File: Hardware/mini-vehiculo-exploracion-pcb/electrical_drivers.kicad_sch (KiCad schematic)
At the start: 13 parts, among them IC1 MAX8891EXK33_V+T, U1 TPS561208DDCR

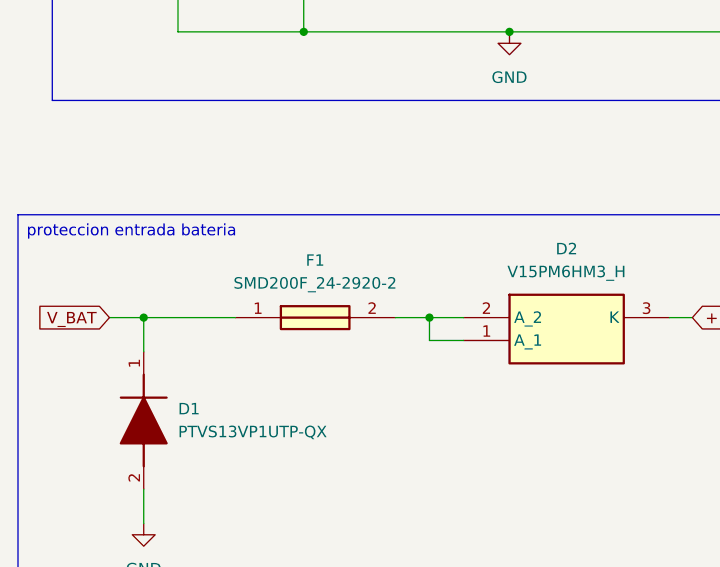
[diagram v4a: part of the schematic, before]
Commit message: actualizacion fusible drivers
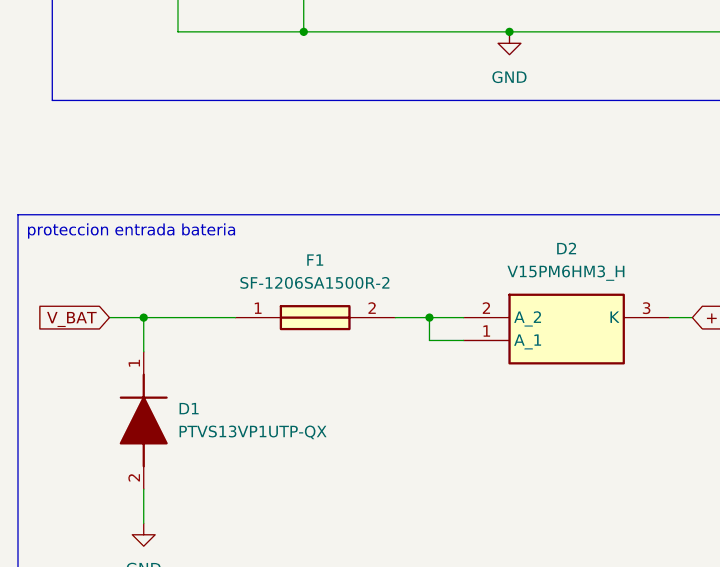
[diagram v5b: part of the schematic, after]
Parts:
- removed F1: SMD200F_24-2920-2, SMD200F2429202, symbol SMD200F_24-2920-2:SMD200F_24-2920-2
- added F1: SF-1206SA1500R-2, SF1206SA1500R2, symbol SF-1206SA1500R-2:SF-1206SA1500R-2
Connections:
- net V_BAT: now also F1.1
- net at D2.1 (A_1), D2.2 (A_2): now also F1.2
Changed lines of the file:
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@@
+	)
+	(symbol
+		(lib_id "SF-1206SA1500R-2:SF-1206SA1500R-2")
+		(at 41.91 96.52 0)
+		(unit 1)
+		(exclude_from_sim no)
+		(in_bom yes)
+		(on_board yes)
+		(dnp no)
+		(fields_autoplaced yes)
+		(property "Reference" "F1"
+			(at 50.8 90.17 0)
+			(effects
+				(font
+					(size 1.27 1.27)
+				)
+			)
+		)
+		(property "Value" "SF-1206SA1500R-2"
+			(at 50.8 92.71 0)
+			(effects
+				(font
+					(size 1.27 1.27)
+				)
+			)
+		)
+		(property "Footprint" "SF1206SA1500R2"
+			(at 55.88 192.71 0)
+			(effects
+				(font
+					(size 1.27 1.27)
+				)
+				(justify left top)
+				(hide yes)
+			)
+		)
+		(property "Datasheet" "http://www.bourns.com/docs/Product-Datasheets/SF-1206SA-R.pdf"
+			(at 55.88 292.71 0)
+			(effects
+				(font
+					(size 1.27 1.27)
+				)
+				(justify left top)
+				(hide yes)
+			)
+		)
+		(property "Description" "1206 slow-blow met-foil. 15A Auto"
+			(at 41.91 96.52 0)
+			(effects
+				(font
+					(size 1.27 1.27)
+				)
+				(hide yes)
+			)
+		)
+		(property "Height" "0.9"
+			(at 55.88 492.71 0)
+			(effects
+				(font
+					(size 1.27 1.27)
+				)
+				(justify left top)
+				(hide yes)
+			)
+		)
+		(property "Mouser Part Number" "652-SF-1206SA1500R-2"
+			(at 55.88 592.71 0)
+			(effects
+				(font
+					(size 1.27 1.27)
+				)
+				(justify left top)
+				(hide yes)
+			)
+		)
+		(property "Mouser Price/Stock" "https://www.mouser.co.uk/ProductDetail/Bourns/SF-1206SA1500R-2?qs=MyNHzdoqoQLFm73fnRlz0w%3D%3D"
+			(at 55.88 692.71 0)
+			(effects
+				(font
+					(size 1.27 1.27)
+				)
+				(justify left top)
+				(hide yes)
+			)
+		)
+		(property "Manufacturer_Name" "Bourns"
+			(at 55.88 792.71 0)
+			(effects
+				(font
+					(size 1.27 1.27)
+				)
+				(justify left top)
+				(hide yes)
+			)
+		)
+		(property "Manufacturer_Part_Number" "SF-1206SA1500R-2"
+			(at 55.88 892.71 0)
+			(effects
+				(font
+					(size 1.27 1.27)
+				)
+				(justify left top)
+				(hide yes)
+			)
+		)
+		(pin "2"
+		)
+		(pin "1"
+		)
+		(instances
+			(project ""
+				(path "/7776e3ee-622a-4a3e-a213-279f6f5df2cb/a0a3a615-a0eb-4e9b-a594-71f734cb4e88"
+					(reference "F1")
+					(unit 1)
+				)
+			)
+		)
 	)
 	(symbol
@@
 					(unit 1)
 				)
-			)
-		)
-	)
-	(symbol
-		(lib_id "SMD200F_24-2920-2:SMD200F_24-2920-2")
-		(at 41.91 96.52 0)
-		(unit 1)
-		(exclude_from_sim no)
-		(in_bom yes)
-		(on_board yes)
-		(dnp no)
-		(fields_autoplaced yes)
-		(property "Reference" "F1"
-			(at 50.8 90.17 0)
-			(effects
-				(font
-					(size 1.27 1.27)
-				)
-			)
-		)
-		(property "Value" "SMD200F_24-2920-2"
-			(at 50.8 92.71 0)
-			(effects
-				(font
-					(size 1.27 1.27)
-				)
-			)
-		)
-		(property "Footprint" "SMD200F2429202"
-			(at 55.88 192.71 0)
-			(effects
-				(font
-					(size 1.27 1.27)
-				)
-				(justify left top)
-				(hide yes)
-			)
-		)
-		(property "Datasheet" "https://www.littelfuse.com/media?resourcetype=datasheets&itemid=e664881a-0c68-4836-928b-7ed2f0c2a6da&filename=littelfuse-ptc-smd-datasheet"
-			(at 55.88 292.71 0)
-			(effects
-				(font
-					(size 1.27 1.27)
-				)
-				(justify left top)
-				(hide yes)
-			)
-		)
-		(property "Description" "LITTELFUSE - SMD200F/24-2920-2 - Resettable Fuse, PPTC, 2920 (7351 Metric), PolySwitch SMD Series, 24 VDC, 2 A, 4 A, 5 s"
-			(at 41.91 96.52 0)
-			(effects
-				(font
-					(size 1.27 1.27)
-				)
-				(hide yes)
-			)
-		)
-		(property "Height" "3"
-			(at 55.88 492.71 0)
-			(effects
-				(font
-					(size 1.27 1.27)
-				)
-				(justify left top)
-				(hide yes)
-			)
-		)
-		(property "Mouser Part Number" "650-SMD200F/2429202"
-			(at 55.88 592.71 0)
-			(effects
-				(font
-					(size 1.27 1.27)
-				)
-				(justify left top)
-				(hide yes)
-			)
-		)
-		(property "Mouser Price/Stock" "https://www.mouser.co.uk/ProductDetail/Littelfuse/SMD200F-24-2920-2?qs=WTEd434rUSU6D3j%2FZW4mUA%3D%3D"
-			(at 55.88 692.71 0)
-			(effects
-				(font
-					(size 1.27 1.27)
-				)
-				(justify left top)
-				(hide yes)
-			)
-		)
-		(property "Manufacturer_Name" "LITTELFUSE"
-			(at 55.88 792.71 0)
-			(effects
-				(font
-					(size 1.27 1.27)
-				)
-				(justify left top)
-				(hide yes)
-			)
-		)
-		(property "Manufacturer_Part_Number" "SMD200F/24-2920-2"
-			(at 55.88 892.71 0)
-			(effects
-				(font
-					(size 1.27 1.27)
-				)
-				(justify left top)
-				(hide yes)
-			)
-		)
-		(pin "2"
-		)
-		(pin "1"
-		)
-		(instances
-			(project ""
-				(path "/7776e3ee-622a-4a3e-a213-279f6f5df2cb/a0a3a615-a0eb-4e9b-a594-71f734cb4e88"
-					(reference "F1")
-					(unit 1)
-				)

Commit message: updated pcb drv
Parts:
- renumbered C5 to C13, U1 to U3
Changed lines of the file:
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@@
 		(dnp no)
 		(fields_autoplaced yes)
-		(property "Reference" "U1"
+		(property "Reference" "U3"
 			(at 64.77 31.75 0)
 			(effects
@@
 			(project ""
 				(path "/7776e3ee-622a-4a3e-a213-279f6f5df2cb/a0a3a615-a0eb-4e9b-a594-71f734cb4e88"
-					(reference "U1")
+					(reference "U3")
 					(unit 1)
 				)
@@
 		(dnp no)
 		(fields_autoplaced yes)
-		(property "Reference" "#PWR014"
+		(property "Reference" "#PWR013"
 			(at 31.75 125.73 0)
 			(effects
@@
 			(project ""
 				(path "/7776e3ee-622a-4a3e-a213-279f6f5df2cb/a0a3a615-a0eb-4e9b-a594-71f734cb4e88"
-					(reference "#PWR014")
+					(reference "#PWR013")
 					(unit 1)
 				)
@@
 		(dnp no)
 		(fields_autoplaced yes)
-		(property "Reference" "#PWR013"
+		(property "Reference" "#PWR014"
 			(at 72.39 71.12 0)
 			(effects
@@
 			(project ""
 				(path "/7776e3ee-622a-4a3e-a213-279f6f5df2cb/a0a3a615-a0eb-4e9b-a594-71f734cb4e88"
-					(reference "#PWR013")
+					(reference "#PWR014")
 					(unit 1)
 				)
@@
 		(dnp no)
 		(fields_autoplaced yes)
-		(property "Reference" "C5"
+		(property "Reference" "C13"
 			(at 39.37 50.7999 0)
 			(effects
@@
 			(project ""
 				(path "/7776e3ee-622a-4a3e-a213-279f6f5df2cb/a0a3a615-a0eb-4e9b-a594-71f734cb4e88"
-					(reference "C5")
-					(unit 1)
-				)
+					(reference "C13")
+					(unit 1)
+				)

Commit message: cambios
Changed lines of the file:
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@@
+	)
+	(junction
+		(at 31.75 119.38)
+		(diameter 0)
+		(color 0 0 0 0)
 	)
 	(junction
@@
 	)
 	(symbol
+		(lib_id "power:PWR_FLAG")
+		(at 31.75 96.52 0)
+		(unit 1)
+		(exclude_from_sim no)
+		(in_bom yes)
+		(on_board yes)
+		(dnp no)
+		(fields_autoplaced yes)
+		(property "Reference" "#FLG01"
+			(at 31.75 94.615 0)
+			(effects
+				(font
+					(size 1.27 1.27)
+				)
+				(hide yes)
+			)
+		)
+		(property "Value" "PWR_FLAG"
+			(at 31.75 91.44 0)
+			(effects
+				(font
+					(size 1.27 1.27)
+				)
+			)
+		)
+		(property "Footprint" ""
+			(at 31.75 96.52 0)
+			(effects
+				(font
+					(size 1.27 1.27)
+				)
+				(hide yes)
+			)
+		)
+		(property "Datasheet" "~"
+			(at 31.75 96.52 0)
+			(effects
+				(font
+					(size 1.27 1.27)
+				)
+				(hide yes)
+			)
+		)
+		(property "Description" "Special symbol for telling ERC where power comes from"
+			(at 31.75 96.52 0)
+			(effects
+				(font
+					(size 1.27 1.27)
+				)
+				(hide yes)
+			)
+		)
+		(pin "1"
+		)
+		(instances
+			(project ""
+				(path "/7776e3ee-622a-4a3e-a213-279f6f5df2cb/a0a3a615-a0eb-4e9b-a594-71f734cb4e88"
+					(reference "#FLG01")
+					(unit 1)
+				)
+			)
+		)
+	)
+	(symbol
 		(lib_id "Device:C")
 		(at 123.19 50.8 0)
@@
 					(unit 1)
 				)
+			)
+		)
+	)
+	(symbol
+		(lib_id "power:PWR_FLAG")
+		(at 31.75 119.38 270)
+		(unit 1)
+		(exclude_from_sim no)
+		(in_bom yes)
+		(on_board yes)
+		(dnp no)
+		(fields_autoplaced yes)
+		(property "Reference" "#FLG02"
+			(at 33.655 119.38 0)
+			(effects
+				(font
+					(size 1.27 1.27)
+				)
+				(hide yes)
+			)
+		)
+		(property "Value" "PWR_FLAG"
+			(at 35.56 119.3799 90)
+			(effects
+				(font
+					(size 1.27 1.27)
+				)
+				(justify left)
+			)
+		)
+		(property "Footprint" ""
+			(at 31.75 119.38 0)
+			(effects
+				(font
+					(size 1.27 1.27)
+				)
+				(hide yes)
+			)
+		)
+		(property "Datasheet" "~"
+			(at 31.75 119.38 0)
+			(effects
+				(font
+					(size 1.27 1.27)
+				)
+				(hide yes)
+			)
+		)
+		(property "Description" "Special symbol for telling ERC where power comes from"
+			(at 31.75 119.38 0)
+			(effects
+				(font
+					(size 1.27 1.27)
+				)
+				(hide yes)
+			)
+		)
+		(pin "1"
+		)
+		(instances
+			(project ""
+				(path "/7776e3ee-622a-4a3e-a213-279f6f5df2cb/a0a3a615-a0eb-4e9b-a594-71f734cb4e88"
+					(reference "#FLG02")
+					(unit 1)
+				)

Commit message: changes etc
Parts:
- C13, C14, C15, C16, C17: footprint (none) -> Capacitor_SMD:C_0805_2012Metric_Pad1.18x1.45mm_HandSolder
- D1: footprint SODFL4725X110N -> PTVS13VP1UTP-QX:SODFL4725X110N
- D2: footprint V15PM6HM3H -> V15PM6HM3_H:V15PM6HM3H
- F1: footprint SF1206SA1500R2 -> SF-1206SA1500R-2:SF1206SA1500R2
- IC1: footprint SOT65P210X110-5N -> MAX8891EXK33_V+T:SOT65P210X110-5N
- R7, R8: footprint (none) -> Resistor_SMD:R_0805_2012Metric_Pad1.20x1.40mm_HandSolder
- U3: footprint SOT95P280X110-6N -> TPS561208DDCR:SOT95P280X110-6N
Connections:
- net GND: now also C16.2, C17.2, IC1.2 (GND)
